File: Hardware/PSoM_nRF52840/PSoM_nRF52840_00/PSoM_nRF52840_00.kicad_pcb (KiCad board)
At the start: 6 copper layers, 26.3 x 23.2 mm, 61 parts, among them J1 Bare PCB USB C, J101 DF40C-60DP-0.4V(51), J102 Bare PCB USB C, J401 Conn_01x01_Pin, J402 Conn_01x01_Pin, SW461 SW_Push, U201 NPM1300-QEAA-R, U401 nRF52840-QIAA-aQFN73, Y401 830108161301

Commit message: working on the routing
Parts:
- removed J102: Bare PCB USB C, Component_lib:usb-c-pcb
- C407: moved to B.Cu
- moved R461 24.1 mm to (135.7, 103.3)
- moved J1 12.0 mm to (130.1, 109.0), turned to 180 degrees
- moved C407 2.38 mm to (131.9, 101.7), turned to -90 degrees
- moved C416 0.84 mm to (139.7, 97.3)
- moved C408 0.53 mm to (130.0, 99.8)
- moved C415 0.42 mm to (140.1, 98.0)
- moved C414 0.42 mm to (140.1, 99.7)
- moved C413 0.42 mm to (137.1, 94.7)
- moved C412 0.41 mm to (136.2, 94.2)
- moved C405 0.32 mm to (139.4, 100.2)
- moved L202 0.11 mm to (141.6, 92.5)
- moved L201 0.06 mm to (144.4, 92.5)
- moved C202 0.06 mm to (143.7, 93.7)
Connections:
- C207 pad 1: /200_1S_Charger/3V3_nRF -> +3V3
- C208 pad 1: +3V3 -> /200_1S_Charger/3V3_nRF
- L201 pad 1: /200_1S_Charger/3V3_nRF -> +3V3
- L202 pad 1: +3V3 -> /200_1S_Charger/3V3_nRF
- R461 pad 1: +3V3 -> /200_1S_Charger/3V3_nRF
- U201 pad 1: /200_1S_Charger/3V3_nRF -> +3V3
- U201 pad 32: +3V3 -> /200_1S_Charger/3V3_nRF
- U401 pad T2: P35 -> P37
- U401 pad U1: P37 -> P35
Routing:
- net +3V3: track 1.19 -> 29.3 mm, vias 0 -> 2
- net GND: track 22.1 -> 36.9 mm
- net /200_1S_Charger/3V3_nRF: track 9.44 -> 13.3 mm, vias 1 -> 4
- net /400-nRF52840/DEC4_6: track 4.89 -> 6.01 mm
- net P39: track 6.43 -> 7.11 mm
- net P37: track 5.12 -> 4.47 mm
- net SPI7: track 4.89 -> 5.51 mm

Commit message: nrf52 routing
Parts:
- removed the ANT450 at (128.3, 85.0)
- moved ANT450 31.8 mm to (121.3, 87.9), turned to 180 degrees
- moved C411 0.20 mm to (135.1, 95.0)
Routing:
- net /400-nRF52840/DEC4_6: track 6.01 -> 11.6 mm, vias 1 -> 2
- net /400-nRF52840/DCC: track 0.00 -> 1.60 mm
- net P27: track 13.1 -> 14.3 mm
- net /400-nRF52840/DCC_DEC4: track 0.00 -> 0.99 mm
- net P25: track 11.7 -> 12.4 mm

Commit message: done for today
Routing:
- net /200_1S_Charger/SDA: track 0.00 -> 1.87 mm
- net P27: track 14.3 -> 15.1 mm
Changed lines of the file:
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@@
 	)
 	(segment
-		(start 136.645 106.025)
-		(end 135.64538 106.025)
+		(start 135.19 102.838456)
+		(end 135.01 102.658456)
 		(width 0.1)
 		(layer "In3.Cu")
@@
 	)
 	(segment
-		(start 135.01 97.503341)
-		(end 136.821114 95.692227)
+		(start 136.675 96.6663)
+		(end 136.675 95.838341)
 		(width 0.1)
 		(layer "In3.Cu")
@@
 	)
 	(segment
-		(start 135.19 105.56962)
-		(end 135.19 102.838456)
+		(start 136.675 95.838341)
+		(end 136.821114 95.692227)
 		(width 0.1)
 		(layer "In3.Cu")
@@
 	)
 	(segment
+		(start 135.01 102.658456)
+		(end 135.01 98.3313)
+		(width 0.1)
+		(layer "In3.Cu")
+		(net 14)
+	)
+	(segment
 		(start 135.64538 106.025)
 		(end 135.19 105.56962)
@@
 	)
 	(segment
-		(start 135.01 102.658456)
-		(end 135.01 97.503341)
+		(start 135.19 105.56962)
+		(end 135.19 102.838456)
 		(width 0.1)
 		(layer "In3.Cu")
@@
 	)
 	(segment
-		(start 135.19 102.838456)
-		(end 135.01 102.658456)
+		(start 136.645 106.025)
+		(end 135.64538 106.025)
+		(width 0.1)
+		(layer "In3.Cu")
+		(net 14)
+	)
+	(segment
+		(start 135.01 98.3313)
+		(end 136.675 96.6663)
 		(width 0.1)
 		(layer "In3.Cu")
@@
 	)
 	(segment
-		(start 138.52 96.67)
-		(end 138.195 96.995)
+		(start 137.53462 105.125)
+		(end 137.725 105.31538)
 		(width 0.1)
 		(layer "In3.Cu")
@@
 	)
 	(segment
-		(start 138.195 96.995)
-		(end 137.535 96.995)
+		(start 136.2937 105.125)
+		(end 137.53462 105.125)
 		(width 0.1)
 		(layer "In3.Cu")
@@
 	)
 	(segment
-		(start 135.95 102.523655)
-		(end 135.95 103.54038)
+		(start 137.4237 96.995)
+		(end 135.8 98.6187)
 		(width 0.1)
 		(layer "In3.Cu")
@@
 	)
 	(segment
-		(start 135.8 98.73)
-		(end 135.8 102.373655)
+		(start 137.725 105.695)
+		(end 137.5 105.92)
 		(width 0.1)
 		(layer "In3.Cu")
@@
 	)
 	(segment
-		(start 135.8 102.373655)
-		(end 135.95 102.523655)
+		(start 138.52 96.67)
+		(end 138.195 96.995)
 		(width 0.1)
 		(layer "In3.Cu")
@@
 	)
 	(segment
-		(start 135.95 103.54038)
-		(end 137.725 105.31538)
+		(start 137.725 105.31538)
+		(end 137.725 105.695)
 		(width 0.1)
 		(layer "In3.Cu")
@@
 	)
 	(segment
-		(start 137.725 105.695)
-		(end 137.5 105.92)
+		(start 138.195 96.995)
+		(end 137.4237 96.995)
 		(width 0.1)
 		(layer "In3.Cu")
@@
 	)
 	(segment
-		(start 137.535 96.995)
-		(end 135.8 98.73)
+		(start 135.95 102.523655)
+		(end 135.95 104.7813)
 		(width 0.1)
 		(layer "In3.Cu")
@@
 	)
 	(segment
-		(start 137.725 105.31538)
-		(end 137.725 105.695)
+		(start 135.95 104.7813)
+		(end 136.2937 105.125)
+		(width 0.1)
+		(layer "In3.Cu")
+		(net 20)
+	)
+	(segment
+		(start 135.8 98.6187)
+		(end 135.8 102.373655)
+		(width 0.1)
+		(layer "In3.Cu")
+		(net 20)
+	)
+	(segment
+		(start 135.8 102.373655)
+		(end 135.95 102.523655)
 		(width 0.1)
 		(layer "In3.Cu")
@@
 	)
 	(segment
-		(start 139.4 100.43934)
-		(end 138.228427 99.267767)
+		(start 139.4 104.19038)
+		(end 138.68 103.47038)
 		(width 0.1)
 		(layer "In3.Cu")
@@
 	(segment
 		(start 139.4 104.25)
-		(end 139.4 100.43934)
+		(end 139.4 104.19038)
+		(width 0.1)
+		(layer "In3.Cu")
+		(net 29)
+	)
+	(segment
+		(start 138.68 103.47038)
+		(end 138.68 99.71934)
+		(width 0.1)
+		(layer "In3.Cu")
+		(net 29)
+	)
+	(segment
+		(start 138.68 99.71934)
+		(end 138.228427 99.267767)
 		(width 0.1)
 		(layer "In3.Cu")
@@
 	)
 	(segment
-		(start 135.57 102.681056)
-		(end 135.57 104.9387)
+		(start 136.16 105.528701)
+		(end 136.271299 105.64)
 		(width 0.1)
 		(layer "In3.Cu")
@@
 	)
 	(segment
-		(start 136.271299 105.64)
-		(end 136.73038 105.64)
+		(start 136.86538 105.775)
+		(end 137.13462 105.775)
 		(width 0.1)
 		(layer "In3.Cu")
@@
 	)
 	(segment
-		(start 136.1 95.05)
-		(end 136.638507 95.05)
+		(start 135.4 98.4813)
+		(end 135.4 102.511056)
 		(width 0.1)
 		(layer "In3.Cu")
@@
 	)
 	(segment
-		(start 136.86538 105.775)
-		(end 137.13462 105.775)
+		(start 135.57 102.681056)
+		(end 135.57 104.9387)
 		(width 0.1)
 		(layer "In3.Cu")
@@
 	)
 	(segment
-		(start 136.16 105.528701)
-		(end 136.271299 105.64)
+		(start 137.4 105.50962)
+		(end 137.4 105.45)
 		(width 0.1)
 		(layer "In3.Cu")
@@
 	)
 	(segment
-		(start 135.57 104.9387)
-		(end 136.16 105.528701)
+		(start 136.1 95.05)
+		(end 136.638507 95.05)
 		(width 0.1)
 		(layer "In3.Cu")
@@
 	)
 	(segment
-		(start 135.4 98.10962)
-		(end 135.4 102.511056)
+		(start 137.325 95.736493)
+		(end 137.325 96.5563)
 		(width 0.1)
 		(layer "In3.Cu")
@@
 	)
 	(segment
-		(start 137.325 95.736493)
-		(end 137.325 96.18462)
+		(start 136.271299 105.64)
+		(end 136.73038 105.64)
 		(width 0.1)
 		(layer "In3.Cu")
@@
 	)
 	(segment
-		(start 137.4 105.50962)
-		(end 137.4 105.45)
+		(start 135.57 104.9387)
+		(end 136.16 105.528701)
 		(width 0.1)
 		(layer "In3.Cu")
@@
 	)
 	(segment
-		(start 137.325 96.18462)
-		(end 135.4 98.10962)
+		(start 137.325 96.5563)
+		(end 135.4 98.4813)
 		(width 0.1)
 		(layer "In3.Cu")
@@
 	)
 	(segment
-		(start 130.42 97.93)
-		(end 131 97.35)
+		(start 134.525 106.934622)
+		(end 134.525 107.08462)
 		(width 0.1)
 		(layer "In2.Cu")
@@
 	)
 	(segment
-		(start 132.85 107.3)
-		(end 130.42 104.87)
+		(start 134.32962 107.28)
+		(end 132.83 107.28)
 		(width 0.1)
 		(layer "In2.Cu")
@@
 	)
 	(segment
-		(start 134.30962 107.3)
-		(end 132.85 107.3)
+		(start 135.109622 106.35)
+		(end 134.525 106.934622)
 		(width 0.1)
 		(layer "In2.Cu")
@@
 	)
 	(segment
-		(start 130.42 104.87)
-		(end 130.42 97.93)
+		(start 135.7 106.35)
+		(end 135.109622 106.35)
 		(width 0.1)
 		(layer "In2.Cu")
@@
 	)
 	(segment
-		(start 134.525 106.934622)
-		(end 134.525 107.08462)
+		(start 130.42 97.93)
+		(end 131 97.35)
 		(width 0.1)
 		(layer "In2.Cu")
@@
 	)
 	(segment
-		(start 135.109622 106.35)
-		(end 134.525 106.934622)
+		(start 134.525 107.08462)
+		(end 134.32962 107.28)
 		(width 0.1)
 		(layer "In2.Cu")
@@
 	)
 	(segment
-		(start 135.7 106.35)
-		(end 135.109622 106.35)
+		(start 132.83 107.28)
+		(end 130.42 104.87)
 		(width 0.1)
 		(layer "In2.Cu")
@@
 	)
 	(segment
-		(start 134.525 107.08462)
-		(end 134.30962 107.3)
+		(start 130.42 104.87)
+		(end 130.42 97.93)
 		(width 0.1)
 		(layer "In2.Cu")
@@
 	)
 	(segment
-		(start 135.38 102.759756)
-		(end 135.2 102.579756)
+		(start 137 96.61)
+		(end 137 96.05)
 		(width 0.1)
 		(layer "In3.Cu")
@@
 	)
 	(segment
-		(start 135.38 105.3)
-		(end 135.38 102.759756)
+		(start 135.2 98.41)
+		(end 137 96.61)
+		(width 0.1)
+		(layer "In3.Cu")
+		(net 48)
+	)
+	(segment
+		(start 135.38 102.759756)
+		(end 135.2 102.579756)
 		(width 0.1)
 		(layer "In3.Cu")
@@
 	(segment
 		(start 135.2 102.579756)
-		(end 135.2 97.85)
+		(end 135.2 98.41)
 		(width 0.1)
 		(layer "In3.Cu")
@@
 	)
 	(segment
-		(start 135.2 97.85)
-		(end 137 96.05)
+		(start 135.38 105.3)
+		(end 135.38 102.759756)
 		(width 0.1)
 		(layer "In3.Cu")
@@
 	)
 	(segment
+		(start 139.619566 97.929527)
+		(end 139.289565 97.929527)
+		(width 0.1)
+		(layer "F.Cu")
+		(net 68)
+	)
+	(segment
+		(start 139.289565 97.929527)
+		(end 138.92 98.299092)
+		(width 0.1)
+		(layer "F.Cu")
+		(net 68)
+	)
+	(segment
+		(start 138.92 98.299092)
+		(end 138.92 98.81)
+		(width 0.1)
+		(layer "F.Cu")
+		(net 68)
+	)
+	(segment
+		(start 138.92 98.81)
+		(end 138.56 99.17)
+		(width 0.1)
+		(layer "F.Cu")
+		(net 68)
+	)
+	(segment
 		(start 143.3775 101.317461)
 		(end 143.3775 101.53)
@@
 	)
 	(segment
-		(start 138.515495 98.556847)
-		(end 138.546215 98.587567)
+		(start 138.525319 98.558538)
+		(end 138.523628 98.556847)
 		(width 0.5)
 		(layer "F.Cu")
@@
 	)
 	(segment
-		(start 136.956847 98.556847)
-		(end 138.515495 98.556847)
+		(start 138.523628 98.556847)
+		(end 136.956847 98.556847)
 		(width 0.5)
 		(layer "F.Cu")
@@
 	)
 	(via
-		(at 138.546215 98.587567)
+		(at 138.525319 98.558538)
 		(size 0.5)
 		(drill 0.2)

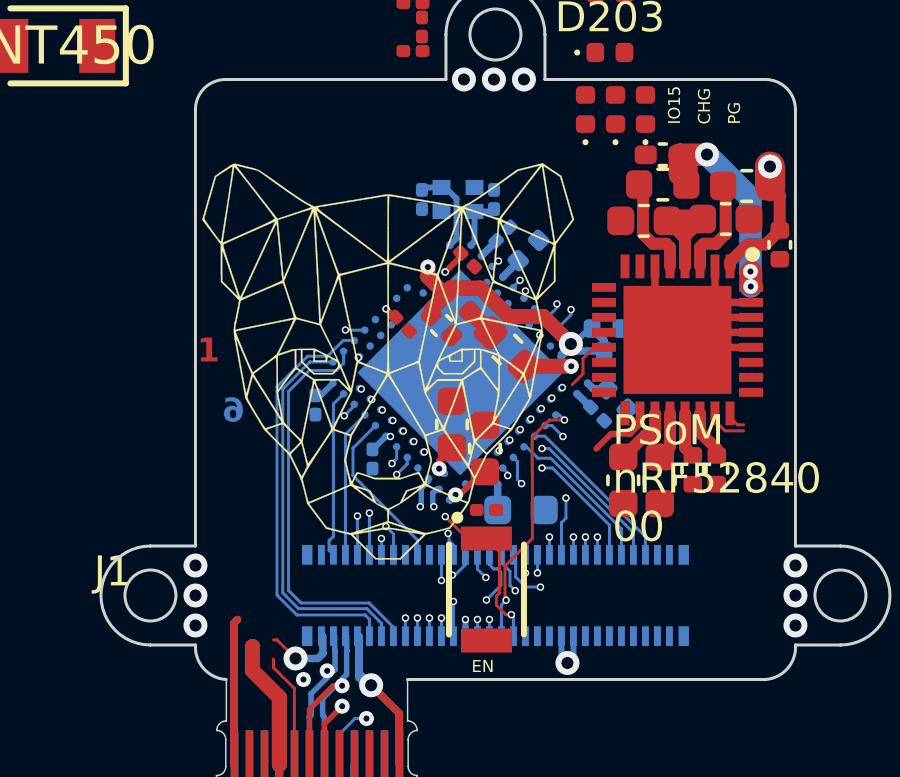
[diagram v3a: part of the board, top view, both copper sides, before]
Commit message: moved the nrf away from the npm
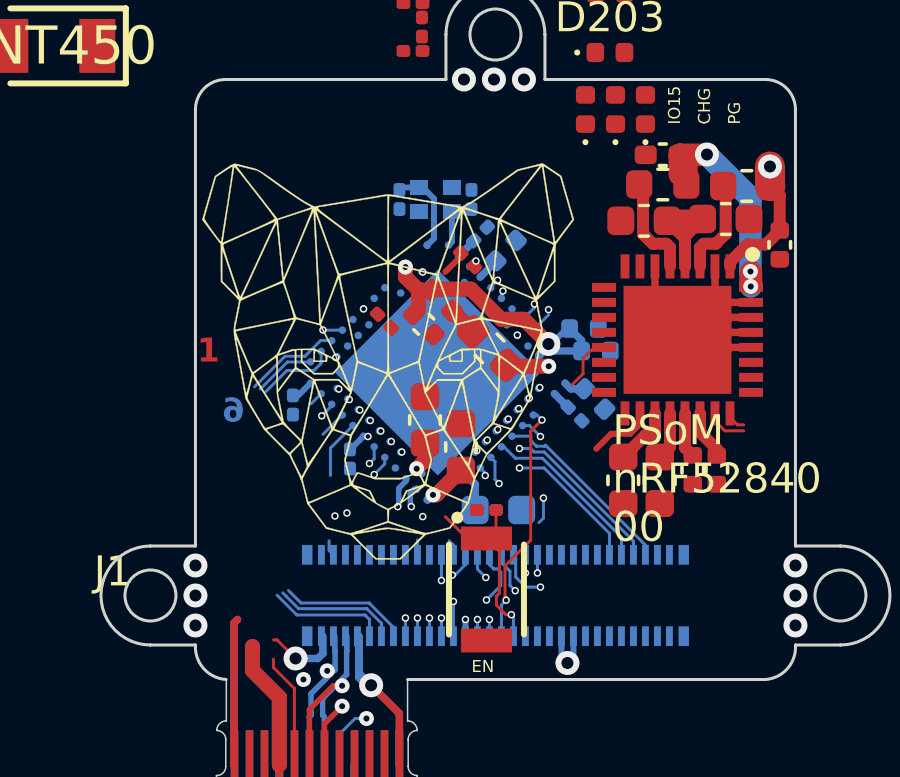
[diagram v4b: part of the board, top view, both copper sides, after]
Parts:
- moved C420 0.91 mm to (133.7, 100.3)
- moved C421 0.80 mm to (134.8, 101.2)
- moved C401 0.75 mm to (132.8, 93.0)
- moved C402 0.75 mm to (135.2, 93.0)
- moved C405 0.75 mm to (138.7, 100.2)
- moved C406 0.75 mm to (136.1, 103.3)
- moved C407 0.75 mm to (131.2, 101.7)
- moved C408 0.75 mm to (129.2, 99.8)
- moved C412 0.75 mm to (135.5, 94.2)
- moved C413 0.75 mm to (136.3, 94.7)
- moved C414 0.75 mm to (139.3, 99.7)
- moved C415 0.75 mm to (139.3, 98.0)
- moved C416 0.75 mm to (138.9, 97.3)
- moved U401 0.75 mm to (134.1, 98.8)
- moved Y401 0.75 mm to (134.0, 93.0)
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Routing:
- net P52: track 14.1 -> 7.19 mm
- net P31: track 17.1 -> 10.2 mm
- net /100_Connectors/SWDIO: track 13.0 -> 6.19 mm
- net /100_Connectors/SWDCLK: track 13.6 -> 6.93 mm
- net P13: track 6.12 -> 0.00 mm, vias 2 -> 0
- net P15: track 5.75 -> 0.00 mm, vias 2 -> 0
- net P46: track 10.8 -> 5.10 mm
- net P17: track 7.86 -> 2.25 mm, vias 2 -> 1
- net SPI0: track 5.63 -> 1.01 mm
- net /200_1S_Charger/SDA: track 1.87 -> 6.32 mm, vias 0 -> 1
- net P42: track 9.14 -> 5.08 mm
- net SPI1: track 4.93 -> 0.91 mm
- net P44: track 9.90 -> 5.99 mm
- net /200_1S_Charger/SCL: track 0.00 -> 3.51 mm, vias 0 -> 1
- net P36: track 7.38 -> 4.31 mm
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
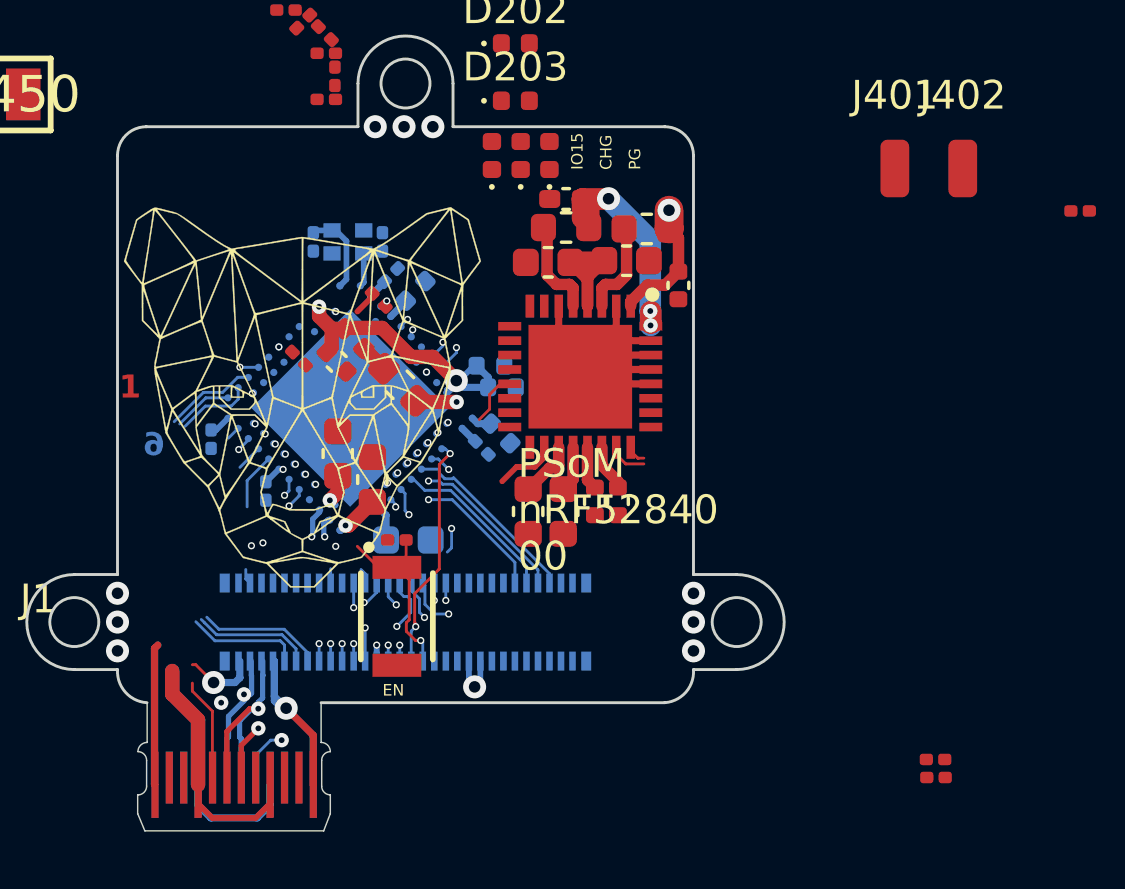
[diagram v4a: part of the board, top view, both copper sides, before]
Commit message: moved the nrf away and re routed everything
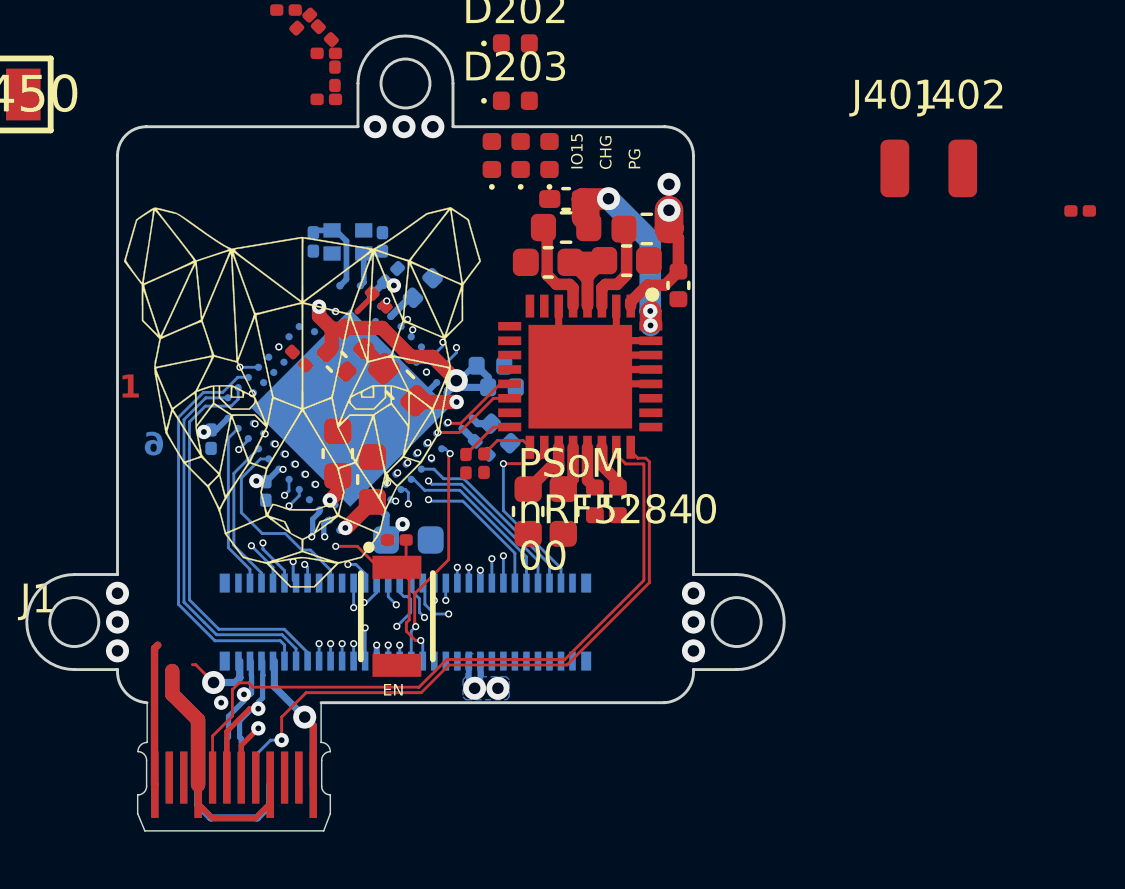
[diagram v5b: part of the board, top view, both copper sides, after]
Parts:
- moved R204 19.3 mm to (138.1, 100.7), turned to -90 degrees
- moved R203 19.1 mm to (138.7, 100.7), turned to -90 degrees
- moved C413 0.27 mm to (136.6, 94.6)
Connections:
- U201 pad 13: /200_1S_Charger/SDA -> P13
- U201 pad 14: /200_1S_Charger/SCL -> P15
- U401 pad D2: /200_1S_Charger/SDA -> P13
- U401 pad F2: /200_1S_Charger/SCL -> P15
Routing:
- net /100_Connectors/CC1: track 4.91 -> 24.7 mm
- net /100_Connectors/CC2: track 5.81 -> 25.3 mm
- net P13: track 0.00 -> 9.38 mm, vias 0 -> 2
- net P15: track 0.00 -> 9.28 mm, vias 0 -> 2
- net P31: track 10.2 -> 17.4 mm
- net P52: track 7.19 -> 14.3 mm
- net /100_Connectors/SWDIO: track 6.19 -> 13.2 mm
- net /100_Connectors/SWDCLK: track 6.93 -> 13.7 mm
- net /200_1S_Charger/SDA: track 6.32 -> 0.00 mm, vias 1 -> 0
- net P46: track 5.10 -> 11.0 mm
- net P17: track 2.25 -> 8.12 mm, vias 1 -> 2
- net P44: track 5.99 -> 11.1 mm
- net SPI0: track 1.01 -> 5.82 mm
- net P42: track 5.08 -> 9.63 mm
- net SPI1: track 0.91 -> 5.41 mm
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- added copper zone on B.Cu, net +3V3

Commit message: TODO: RF and GND vias
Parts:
- removed C101: 100n, Capacitor_SMD:C_0201_0603Metric
- removed the D201 at (141.0, 90.0)
- removed the D202 at (140.0, 90.0)
- removed D461: LED, LED_SMD:LED_0402_1005Metric
- removed R101: 220k, Resistor_SMD:R_0201_0603Metric
- removed R102: 470k, Resistor_SMD:R_0201_0603Metric
- removed R462: 2k, Resistor_SMD:R_0402_1005Metric
- removed SHIPHLD1: TestPoint, TestPoint:TestPoint_Pad_D1.0mm
- added R205: 10k, Resistor_SMD:R_0201_0603Metric, B.Cu at (140.0, 98.5)
- moved J402 28.6 mm to (127.2, 95.5), turned to 90 degrees
- moved J401 26.5 mm to (127.2, 96.8), turned to 90 degrees
- moved C461 25.3 mm to (137.0, 103.5), turned to 90 degrees
- moved ANT450 7.92 mm to (128.8, 90.5)
- moved C403 7.47 mm to (131.2, 95.2)
- moved L401 7.29 mm to (131.5, 94.2)
- moved C404 7.09 mm to (131.2, 93.2)
- moved C451 6.66 mm to (131.8, 92.2), turned to -90 degrees
- moved D201 5.94 mm to (139.0, 90.0), turned to -90 degrees
- moved L452 5.90 mm to (132.2, 91.2), turned to 0 degrees
- moved L451 5.57 mm to (131.4, 90.5), turned to -45 degrees
- moved D202 3.89 mm to (140.0, 90.0), turned to -90 degrees
- moved C401 2.80 mm to (134.7, 90.9), turned to -135 degrees
- moved D203 2.24 mm to (141.0, 90.0), turned to -90 degrees
- moved Y401 1.95 mm to (135.5, 91.8), turned to -135 degrees
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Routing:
- net /200_1S_Charger/3V3_nRF: track 15.1 -> 58.9 mm, vias 8 -> 9
- net /100_Connectors/VSYS: track 6.38 -> 35.6 mm, vias 0 -> 6
- net VBUS: track 18.6 -> 42.4 mm, vias 0 -> 3
- net /200_1S_Charger/LED0: track 0.00 -> 13.0 mm, vias 0 -> 2
- net /200_1S_Charger/LED1: track 0.00 -> 12.0 mm, vias 0 -> 2
- net /200_1S_Charger/LED2: track 0.00 -> 11.2 mm, vias 0 -> 2
- net /200_1S_Charger/VBUS_OUT: track 3.16 -> 13.5 mm, vias 1 -> 2
- net /100_Connectors/D-: track 8.61 -> 16.2 mm
- net /100_Connectors/VBAT: track 2.03 -> 8.98 mm, vias 0 -> 1
- net /100_Connectors/D+: track 8.60 -> 15.4 mm
- net /400-nRF52840/NFC2: track 0.00 -> 5.24 mm, vias 0 -> 1
- net /400-nRF52840/NFC1: track 0.00 -> 4.91 mm, vias 0 -> 1
- net /400-nRF52840/ANT_MATCH: track 0.00 -> 2.65 mm
- net /400-nRF52840/LNA_IN: track 0.00 -> 2.50 mm, vias 0 -> 1
- net /400-nRF52840/XC1: track 3.00 -> 5.01 mm
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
